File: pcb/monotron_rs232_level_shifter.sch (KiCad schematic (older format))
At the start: 7 parts, among them J9 DB9_Male, U3 MAX3232

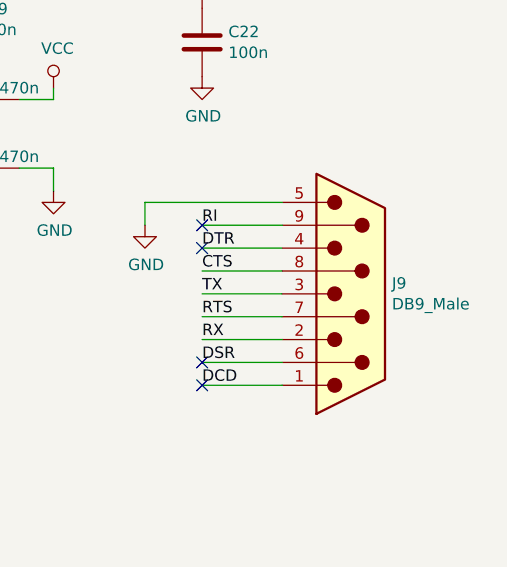
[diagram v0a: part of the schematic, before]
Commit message: Added I/O, RS232 and VGA interfaces. Just audio to add.
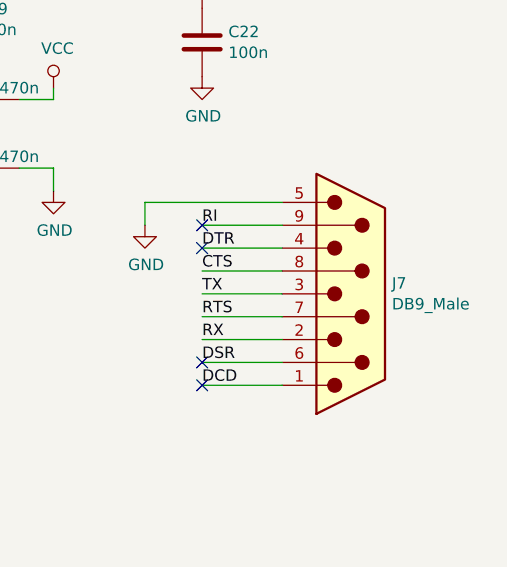
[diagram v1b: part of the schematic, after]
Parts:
- renumbered J9 to J7
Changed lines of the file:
@@
 $Descr A4 11693 8268
 encoding utf-8
-Sheet 2 2
+Sheet 2 3
 Title "Monotron 32K RS-232 Interface"
 Date "2018-12-29"
@@
 $EndComp
 $Comp
-L Connector:DB9_Male J9
+L Connector:DB9_Male J7
 U 1 1 5C526711
 P 6950 3650
-F 0 "J9" H 7130 3696 50  0000 L CNN
+F 0 "J7" H 7130 3696 50  0000 L CNN
 F 1 "DB9_Male" H 7130 3605 50  0000 L CNN
 F 2 "" H 6950 3650 50  0001 C CNN
@@
 	3050 3900 3400 3900
 $Comp
-L power:GND #PWR021
+L power:GND #PWR025
 U 1 1 5C54CA78
 P 4200 4550
-F 0 "#PWR021" H 4200 4300 50  0001 C CNN
+F 0 "#PWR025" H 4200 4300 50  0001 C CNN
 F 1 "GND" H 4205 4377 50  0000 C CNN
 F 2 "" H 4200 4550 50  0001 C CNN
@@
 	3200 2600 3400 2600
 $Comp
-L power:GND #PWR023
+L power:GND #PWR027
 U 1 1 5C54D3EE
 P 5650 3200
-F 0 "#PWR023" H 5650 2950 50  0001 C CNN
+F 0 "#PWR027" H 5650 2950 50  0001 C CNN
 F 1 "GND" H 5655 3027 50  0000 C CNN
 F 2 "" H 5650 3200 50  0001 C CNN
@@
 $EndComp
 $Comp
-L power:VCC #PWR022
+L power:VCC #PWR026
 U 1 1 5C54D461
 P 5650 2750
-F 0 "#PWR022" H 5650 2600 50  0001 C CNN
+F 0 "#PWR026" H 5650 2600 50  0001 C CNN
 F 1 "VCC" H 5667 2923 50  0000 C CNN
 F 2 "" H 5650 2750 50  0001 C CNN
@@
 	5650 3100 5650 3200
 $Comp
-L power:GND #PWR024
+L power:GND #PWR028
 U 1 1 5C54F305
 P 6050 3350
-F 0 "#PWR024" H 6050 3100 50  0001 C CNN
+F 0 "#PWR028" H 6050 3100 50  0001 C CNN
 F 1 "GND" H 6055 3177 50  0000 C CNN
 F 2 "" H 6050 3350 50  0001 C CNN
@@
 CTS
 $Comp
-L power:VCC #PWR020
+L power:VCC #PWR024
 U 1 1 5C553FD8
 P 4200 1950
-F 0 "#PWR020" H 4200 1800 50  0001 C CNN
+F 0 "#PWR024" H 4200 1800 50  0001 C CNN
 F 1 "VCC" H 4217 2123 50  0000 C CNN
 F 2 "" H 4200 1950 50  0001 C CNN
@@
 $EndComp
 $Comp
-L power:VCC #PWR025
+L power:VCC #PWR029
 U 1 1 5C5559B1
 P 6300 2400
-F 0 "#PWR025" H 6300 2250 50  0001 C CNN
+F 0 "#PWR029" H 6300 2250 50  0001 C CNN
 F 1 "VCC" H 6317 2573 50  0000 C CNN
 F 2 "" H 6300 2400 50  0001 C CNN
@@
 $EndComp
 $Comp
-L power:GND #PWR026
+L power:GND #PWR030
 U 1 1 5C5559CA
 P 6300 2700
-F 0 "#PWR026" H 6300 2450 50  0001 C CNN
+F 0 "#PWR030" H 6300 2450 50  0001 C CNN
 F 1 "GND" H 6305 2527 50  0000 C CNN
 F 2 "" H 6300 2700 50  0001 C CNN

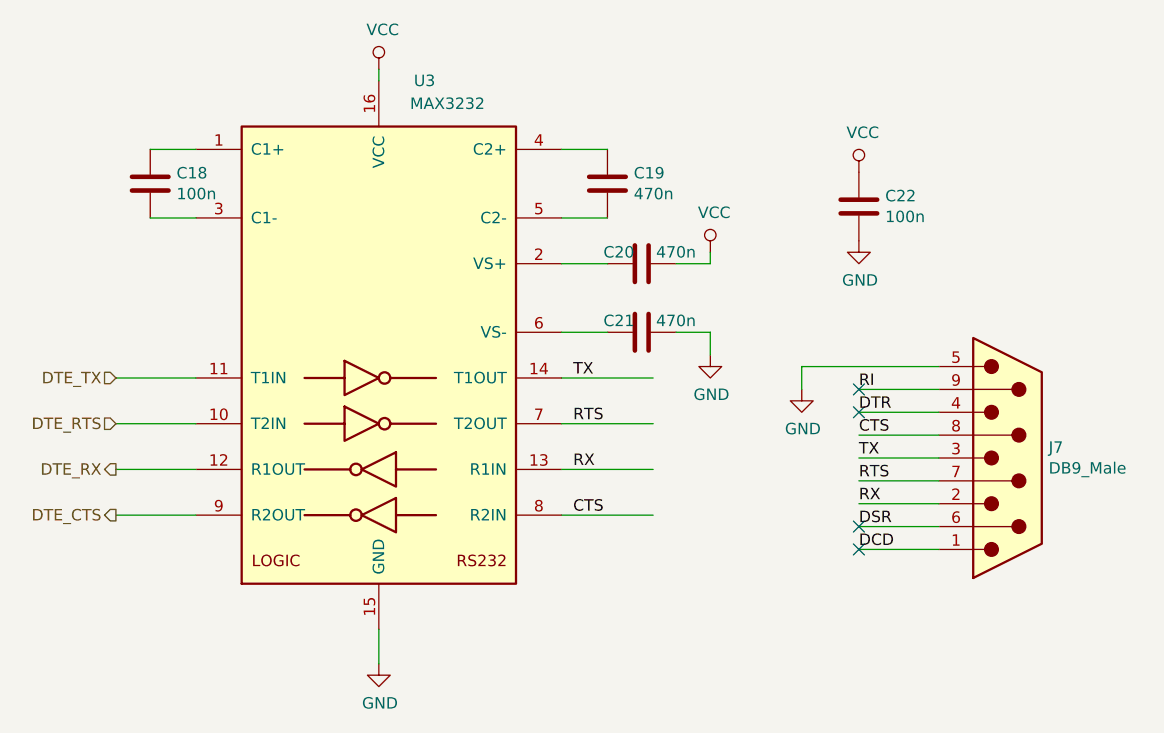
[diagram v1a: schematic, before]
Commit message: Changed to use Launchpad instead of bare chip. PS/2 handled by ATTINY24. LPT handled by MCP23017.
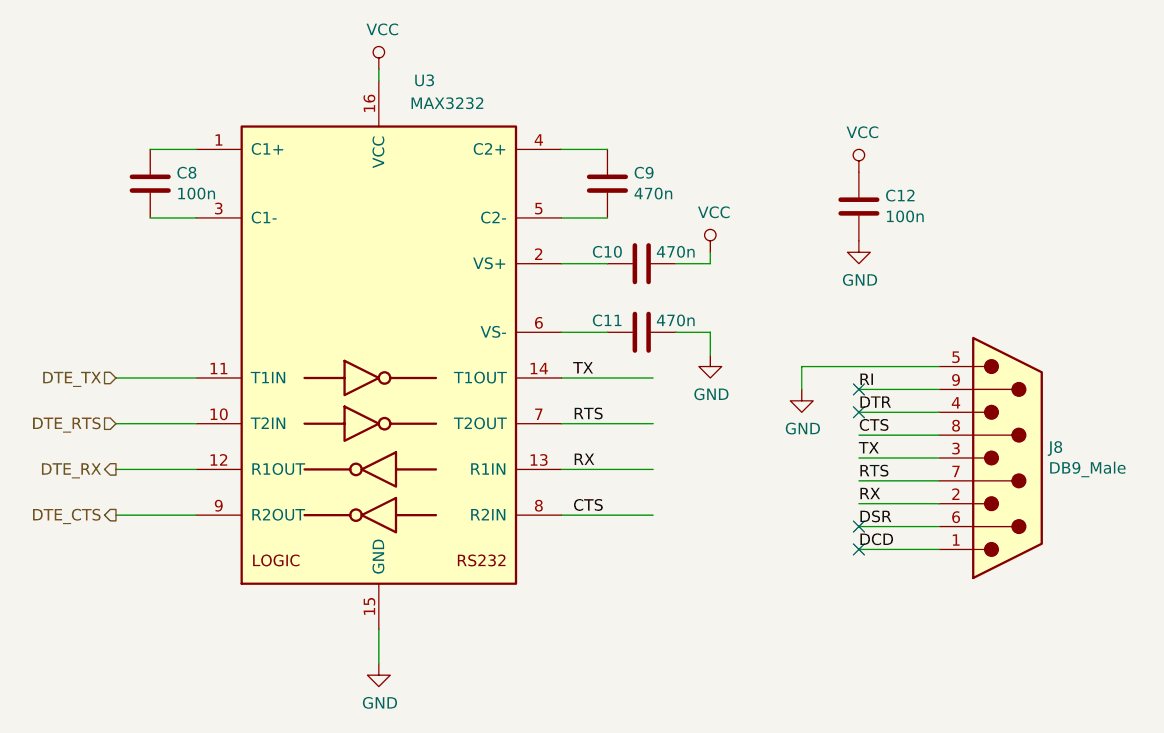
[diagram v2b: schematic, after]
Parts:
- renumbered C20 to C10, C21 to C11, C22 to C12, C18 to C8, C19 to C9, J7 to J8
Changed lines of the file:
@@
 EESchema Schematic File Version 4
+LIBS:monotron-cache
 EELAYER 26 0
 EELAYER END
@@
 $EndComp
 $Comp
-L Connector:DB9_Male J7
+L Connector:DB9_Male J8
 U 1 1 5C526711
 P 6950 3650
-F 0 "J7" H 7130 3696 50  0000 L CNN
+F 0 "J8" H 7130 3696 50  0000 L CNN
 F 1 "DB9_Male" H 7130 3605 50  0000 L CNN
 F 2 "" H 6950 3650 50  0001 C CNN
@@
 	3050 3900 3400 3900
 $Comp
-L power:GND #PWR025
+L power:GND #PWR023
 U 1 1 5C54CA78
 P 4200 4550
-F 0 "#PWR025" H 4200 4300 50  0001 C CNN
+F 0 "#PWR023" H 4200 4300 50  0001 C CNN
 F 1 "GND" H 4205 4377 50  0000 C CNN
 F 2 "" H 4200 4550 50  0001 C CNN
@@
 	4200 4400 4200 4550
 $Comp
-L Device:C C18
+L Device:C C8
 U 1 1 5C54CBB8
 P 3200 2450
-F 0 "C18" H 3315 2496 50  0000 L CNN
+F 0 "C8" H 3315 2496 50  0000 L CNN
 F 1 "100n" H 3315 2405 50  0000 L CNN
 F 2 "" H 3238 2300 50  0001 C CNN
@@
 $EndComp
 $Comp
-L Device:C C19
+L Device:C C9
 U 1 1 5C54CBF3
 P 5200 2450
-F 0 "C19" H 5315 2496 50  0000 L CNN
+F 0 "C9" H 5315 2496 50  0000 L CNN
 F 1 "470n" H 5315 2405 50  0000 L CNN
 F 2 "" H 5238 2300 50  0001 C CNN
@@
 $EndComp
 $Comp
-L Device:C C20
+L Device:C C10
 U 1 1 5C54CC2D
 P 5350 2800
-F 0 "C20" V 5300 2700 50  0000 C CNN
+F 0 "C10" V 5300 2650 50  0000 C CNN
 F 1 "470n" V 5300 2950 50  0000 C CNN
 F 2 "" H 5388 2650 50  0001 C CNN
@@
 $EndComp
 $Comp
-L Device:C C21
+L Device:C C11
 U 1 1 5C54CCB8
 P 5350 3100
-F 0 "C21" V 5300 3000 50  0000 C CNN
+F 0 "C11" V 5300 2950 50  0000 C CNN
 F 1 "470n" V 5300 3250 50  0000 C CNN
 F 2 "" H 5388 2950 50  0001 C CNN
@@
 	3200 2600 3400 2600
 $Comp
-L power:GND #PWR027
+L power:GND #PWR025
 U 1 1 5C54D3EE
 P 5650 3200
-F 0 "#PWR027" H 5650 2950 50  0001 C CNN
+F 0 "#PWR025" H 5650 2950 50  0001 C CNN
 F 1 "GND" H 5655 3027 50  0000 C CNN
 F 2 "" H 5650 3200 50  0001 C CNN
@@
 $EndComp
 $Comp
-L power:VCC #PWR026
+L power:VCC #PWR024
 U 1 1 5C54D461
 P 5650 2750
-F 0 "#PWR026" H 5650 2600 50  0001 C CNN
+F 0 "#PWR024" H 5650 2600 50  0001 C CNN
 F 1 "VCC" H 5667 2923 50  0000 C CNN
 F 2 "" H 5650 2750 50  0001 C CNN
@@
 	5650 3100 5650 3200
 $Comp
-L power:GND #PWR028
+L power:GND #PWR026
 U 1 1 5C54F305
 P 6050 3350
-F 0 "#PWR028" H 6050 3100 50  0001 C CNN
+F 0 "#PWR026" H 6050 3100 50  0001 C CNN
 F 1 "GND" H 6055 3177 50  0000 C CNN
 F 2 "" H 6050 3350 50  0001 C CNN
@@
 CTS
 $Comp
-L power:VCC #PWR024
+L power:VCC #PWR022
 U 1 1 5C553FD8
 P 4200 1950
-F 0 "#PWR024" H 4200 1800 50  0001 C CNN
+F 0 "#PWR022" H 4200 1800 50  0001 C CNN
 F 1 "VCC" H 4217 2123 50  0000 C CNN
 F 2 "" H 4200 1950 50  0001 C CNN
@@
 $EndComp
 $Comp
-L Device:C C22
+L Device:C C12
 U 1 1 5C555922
 P 6300 2550
-F 0 "C22" H 6415 2596 50  0000 L CNN
+F 0 "C12" H 6415 2596 50  0000 L CNN
 F 1 "100n" H 6415 2505 50  0000 L CNN
 F 2 "" H 6338 2400 50  0001 C CNN
@@
 $EndComp
 $Comp
-L power:VCC #PWR029
+L power:VCC #PWR027
 U 1 1 5C5559B1
 P 6300 2400
-F 0 "#PWR029" H 6300 2250 50  0001 C CNN
+F 0 "#PWR027" H 6300 2250 50  0001 C CNN
 F 1 "VCC" H 6317 2573 50  0000 C CNN
 F 2 "" H 6300 2400 50  0001 C CNN
@@
 $EndComp
 $Comp
-L power:GND #PWR030
+L power:GND #PWR028
 U 1 1 5C5559CA
 P 6300 2700
-F 0 "#PWR030" H 6300 2450 50  0001 C CNN
+F 0 "#PWR028" H 6300 2450 50  0001 C CNN
 F 1 "GND" H 6305 2527 50  0000 C CNN
 F 2 "" H 6300 2700 50  0001 C CNN

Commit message: Adding footprints.
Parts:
- C10: renamed from C12; footprint (none) -> Capacitor_THT:C_Disc_D5.0mm_W2.5mm_P2.50mm
- C6: renamed from C8; footprint (none) -> Capacitor_THT:C_Disc_D5.0mm_W2.5mm_P2.50mm
- C7: renamed from C9; footprint (none) -> Capacitor_THT:C_Disc_D5.0mm_W2.5mm_P2.50mm
- C8: renamed from C10; footprint (none) -> Capacitor_THT:C_Disc_D5.0mm_W2.5mm_P2.50mm
- C9: renamed from C11; footprint (none) -> Capacitor_THT:C_Disc_D5.0mm_W2.5mm_P2.50mm
- J8: footprint (none) -> Connector_Dsub:DSUB-9_Male_Horizontal_P2.77x2.84mm_EdgePinOffset7.70mm_Housed_MountingHolesOffset9.12mm; Digikey (none) -> 609-5918-ND
- U2: renamed from U3; footprint (none) -> Package_DIP:DIP-16_W7.62mm; Digikey (none) -> ICL3232CPZ-ND
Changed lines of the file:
@@
 $EndDescr
 $Comp
-L Interface_UART:MAX3232 U3
+L Interface_UART:MAX3232 U2
 U 1 1 5C52663D
 P 4200 3200
-F 0 "U3" H 4400 4400 50  0000 C CNN
+F 0 "U2" H 4400 4400 50  0000 C CNN
 F 1 "MAX3232" H 4500 4300 50  0000 C CNN
-F 2 "" H 4250 2150 50  0001 L CNN
-F 3 "https://datasheets.maximintegrated.com/en/ds/MAX3222-MAX3241.pdf" H 4200 3300 50  0001 C CNN
+F 2 "Package_DIP:DIP-16_W7.62mm" H 4250 2150 50  0001 L CNN
+F 3 "http://www.intersil.com/content/dam/Intersil/documents/icl3/icl3221-22-23-32-41-43.pdf" H 4200 3300 50  0001 C CNN
+F 4 "ICL3232CPZ-ND" H 4200 3200 50  0001 C CNN "Digikey"
 	1    4200 3200
 	1    0    0    -1
@@
 F 0 "J8" H 7130 3696 50  0000 L CNN
 F 1 "DB9_Male" H 7130 3605 50  0000 L CNN
-F 2 "" H 6950 3650 50  0001 C CNN
-F 3 " ~" H 6950 3650 50  0001 C CNN
+F 2 "Connector_Dsub:DSUB-9_Male_Horizontal_P2.77x2.84mm_EdgePinOffset7.70mm_Housed_MountingHolesOffset9.12mm" H 6950 3650 50  0001 C CNN
+F 3 "http://portal.fciconnect.com/Comergent//fci/drawing/c-dd-0024.pdf" H 6950 3650 50  0001 C CNN
+F 4 "609-5918-ND" H 6950 3650 50  0001 C CNN "Digikey"
 	1    6950 3650
 	1    0    0    -1
@@
 	3050 3900 3400 3900
 $Comp
-L power:GND #PWR023
+L power:GND #PWR020
 U 1 1 5C54CA78
 P 4200 4550
-F 0 "#PWR023" H 4200 4300 50  0001 C CNN
+F 0 "#PWR020" H 4200 4300 50  0001 C CNN
 F 1 "GND" H 4205 4377 50  0000 C CNN
 F 2 "" H 4200 4550 50  0001 C CNN
@@
 	4200 4400 4200 4550
 $Comp
-L Device:C C8
+L Device:C C6
 U 1 1 5C54CBB8
 P 3200 2450
-F 0 "C8" H 3315 2496 50  0000 L CNN
+F 0 "C6" H 3315 2496 50  0000 L CNN
 F 1 "100n" H 3315 2405 50  0000 L CNN
-F 2 "" H 3238 2300 50  0001 C CNN
+F 2 "Capacitor_THT:C_Disc_D5.0mm_W2.5mm_P2.50mm" H 3238 2300 50  0001 C CNN
 F 3 "~" H 3200 2450 50  0001 C CNN
 	1    3200 2450
@@
 $EndComp
 $Comp
-L Device:C C9
+L Device:C C7
 U 1 1 5C54CBF3
 P 5200 2450
-F 0 "C9" H 5315 2496 50  0000 L CNN
+F 0 "C7" H 5315 2496 50  0000 L CNN
 F 1 "470n" H 5315 2405 50  0000 L CNN
-F 2 "" H 5238 2300 50  0001 C CNN
+F 2 "Capacitor_THT:C_Disc_D5.0mm_W2.5mm_P2.50mm" H 5238 2300 50  0001 C CNN
 F 3 "~" H 5200 2450 50  0001 C CNN
 	1    5200 2450
@@
 $EndComp
 $Comp
-L Device:C C10
+L Device:C C8
 U 1 1 5C54CC2D
 P 5350 2800
-F 0 "C10" V 5300 2650 50  0000 C CNN
+F 0 "C8" V 5300 2650 50  0000 C CNN
 F 1 "470n" V 5300 2950 50  0000 C CNN
-F 2 "" H 5388 2650 50  0001 C CNN
+F 2 "Capacitor_THT:C_Disc_D5.0mm_W2.5mm_P2.50mm" H 5388 2650 50  0001 C CNN
 F 3 "~" H 5350 2800 50  0001 C CNN
 	1    5350 2800
@@
 $EndComp
 $Comp
-L Device:C C11
+L Device:C C9
 U 1 1 5C54CCB8
 P 5350 3100
-F 0 "C11" V 5300 2950 50  0000 C CNN
+F 0 "C9" V 5300 2950 50  0000 C CNN
 F 1 "470n" V 5300 3250 50  0000 C CNN
-F 2 "" H 5388 2950 50  0001 C CNN
+F 2 "Capacitor_THT:C_Disc_D5.0mm_W2.5mm_P2.50mm" H 5388 2950 50  0001 C CNN
 F 3 "~" H 5350 3100 50  0001 C CNN
 	1    5350 3100
@@
 	3200 2600 3400 2600
 $Comp
-L power:GND #PWR025
+L power:GND #PWR022
 U 1 1 5C54D3EE
 P 5650 3200
-F 0 "#PWR025" H 5650 2950 50  0001 C CNN
+F 0 "#PWR022" H 5650 2950 50  0001 C CNN
 F 1 "GND" H 5655 3027 50  0000 C CNN
 F 2 "" H 5650 3200 50  0001 C CNN
@@
 $EndComp
 $Comp
-L power:VCC #PWR024
+L power:VCC #PWR021
 U 1 1 5C54D461
 P 5650 2750
-F 0 "#PWR024" H 5650 2600 50  0001 C CNN
+F 0 "#PWR021" H 5650 2600 50  0001 C CNN
 F 1 "VCC" H 5667 2923 50  0000 C CNN
 F 2 "" H 5650 2750 50  0001 C CNN
@@
 	5650 3100 5650 3200
 $Comp
-L power:GND #PWR026
+L power:GND #PWR023
 U 1 1 5C54F305
 P 6050 3350
-F 0 "#PWR026" H 6050 3100 50  0001 C CNN
+F 0 "#PWR023" H 6050 3100 50  0001 C CNN
 F 1 "GND" H 6055 3177 50  0000 C CNN
 F 2 "" H 6050 3350 50  0001 C CNN
@@
 CTS
 $Comp
-L power:VCC #PWR022
+L power:VCC #PWR019
 U 1 1 5C553FD8
 P 4200 1950
-F 0 "#PWR022" H 4200 1800 50  0001 C CNN
+F 0 "#PWR019" H 4200 1800 50  0001 C CNN
 F 1 "VCC" H 4217 2123 50  0000 C CNN
 F 2 "" H 4200 1950 50  0001 C CNN
@@
 $EndComp
 $Comp
-L Device:C C12
+L Device:C C10
 U 1 1 5C555922
 P 6300 2550
-F 0 "C12" H 6415 2596 50  0000 L CNN
+F 0 "C10" H 6415 2596 50  0000 L CNN
 F 1 "100n" H 6415 2505 50  0000 L CNN
-F 2 "" H 6338 2400 50  0001 C CNN
+F 2 "Capacitor_THT:C_Disc_D5.0mm_W2.5mm_P2.50mm" H 6338 2400 50  0001 C CNN
 F 3 "~" H 6300 2550 50  0001 C CNN
 	1    6300 2550
@@
 $EndComp
 $Comp
-L power:VCC #PWR027
+L power:VCC #PWR024
 U 1 1 5C5559B1
 P 6300 2400
-F 0 "#PWR027" H 6300 2250 50  0001 C CNN
+F 0 "#PWR024" H 6300 2250 50  0001 C CNN
 F 1 "VCC" H 6317 2573 50  0000 C CNN
 F 2 "" H 6300 2400 50  0001 C CNN
@@
 $EndComp
 $Comp
-L power:GND #PWR028
+L power:GND #PWR025
 U 1 1 5C5559CA
 P 6300 2700
-F 0 "#PWR028" H 6300 2450 50  0001 C CNN
+F 0 "#PWR025" H 6300 2450 50  0001 C CNN
 F 1 "GND" H 6305 2527 50  0000 C CNN
 F 2 "" H 6300 2700 50  0001 C CNN
